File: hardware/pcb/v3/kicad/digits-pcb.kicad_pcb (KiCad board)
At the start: 2 copper layers, 61.9 x 76.2 mm, 77 parts, among them J8 Conn_01x04, SW1 Hook_DPDT, SW2 SW_Push, U10 XL6019E1, U2 DRV8871DDAR, U3 RP2040, U4 W25Q16JVSSIQ, U5 AMS1117-3.3, U6 TLV320AIC3104IRHBR, U7 XC6206P182MR, Y1 ABM8-272-T3

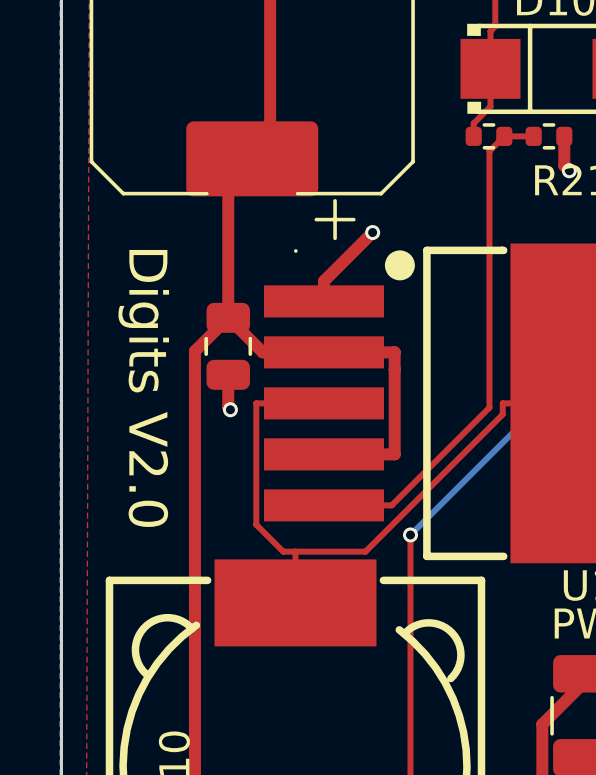
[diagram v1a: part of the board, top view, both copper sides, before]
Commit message: chore(hardware): update board silkscreen version label to V3
The F.SilkS title still read "Digits V2.0" after the promotion to V3.
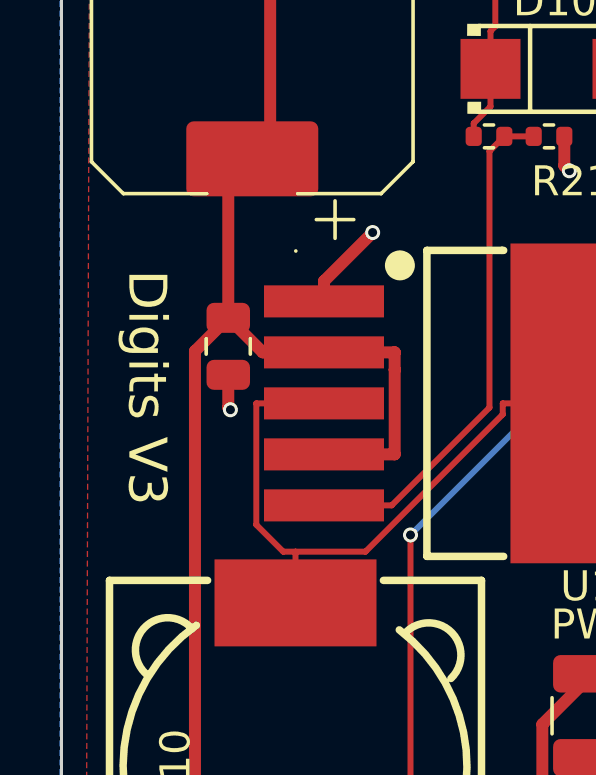
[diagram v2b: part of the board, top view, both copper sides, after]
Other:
- board text added: "Digits V3"
- board text removed: "Digits V2.0"
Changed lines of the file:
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@@
 		)
 	)
-	(gr_text "Digits V2.0"
+	(gr_text "Digits V3"
 		(at 15.598989 48.085455 270)
 		(layer "F.SilkS")

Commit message: fix(hardware): rate C55 for the 37V boost rail, assign SW2 BOOTSEL part
C55 was a 25V electrolytic on VBOOST (37.25V), which would over-volt and
fail. It is local VM decoupling, not the rail source (the XL6019 regulates
37V and C100's 100uF is the bulk reservoir), so dropping it to 10uF/50V
(C116402) in the same 5mm footprint keeps the decoupling ample with no
layout change. Also assign the SW2 6mm tactile (OMRON B3F-1002, C87036)
so the BOOTSEL button places.

DRC stays clean: 0 errors, 0 unconnected, 0 schematic-parity.
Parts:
- C55: value 47uF -> 10uF
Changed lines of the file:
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@@
 			)
 		)
-		(property "LCSC Part #" "C25102"
-			(at 0 0 0)
-			(unlocked yes)
+		(property "Value" "300"
+			(at 0 1.17 0)
 			(layer "F.Fab")
-			(hide yes)
 			(effects
 				(font
@@
 			)
 		)
-		(property "Value" "300"
-			(at 0 1.17 0)
+		(property "Datasheet" "~"
+			(at 0 0 0)
 			(layer "F.Fab")
+			(hide yes)
 			(effects
 				(font
-					(size 1 1)
-					(thickness 0.15)
+					(size 1.27 1.27)
 				)
 			)
 		)
-		(property "Datasheet" "~"
+		(property "Description" ""
 			(at 0 0 0)
 			(layer "F.Fab")
@@
 			)
 		)
-		(property "Description" ""
+		(property "LCSC Part #" "C25102"
 			(at 0 0 0)
+			(unlocked yes)
 			(layer "F.Fab")
 			(hide yes)
 			(effects
 				(font
-					(size 1.27 1.27)
+					(size 1 1)
+					(thickness 0.15)
 				)
 			)
@@
 			)
 		)
-		(property "LCSC Part #" "C2286"
-			(at 0 0 0)
-			(unlocked yes)
+		(property "Value" "LED_RED"
+			(at 0 1.43 0)
 			(layer "F.Fab")
-			(hide yes)
 			(effects
 				(font
@@
 			)
 		)
-		(property "Value" "LED_RED"
-			(at 0 1.43 0)
+		(property "Datasheet" "~"
+			(at 0 0 0)
 			(layer "F.Fab")
+			(hide yes)
 			(effects
 				(font
-					(size 1 1)
-					(thickness 0.15)
+					(size 1.27 1.27)
 				)
 			)
 		)
-		(property "Datasheet" "~"
+		(property "Description" ""
 			(at 0 0 0)
 			(layer "F.Fab")
@@
 			)
 		)
-		(property "Description" ""
+		(property "LCSC Part #" "C2286"
 			(at 0 0 0)
+			(unlocked yes)
 			(layer "F.Fab")
 			(hide yes)
 			(effects
 				(font
-					(size 1.27 1.27)
+					(size 1 1)
+					(thickness 0.15)
 				)
 			)
@@
 			)
 		)
-		(property "Value" "47uF"
+		(property "Value" "10uF"
 			(at 0 -3.7 90)
 			(layer "F.Fab")
@@
 			)
 		)
-		(property "LCSC Part #" "C336270"
+		(property "LCSC Part #" "C116402"
 			(at 0 0 270)
 			(unlocked yes)
@@
 			)
 		)
-		(property "LCSC Part #" "C12624"
-			(at 0 0 0)
-			(unlocked yes)
+		(property "Value" "LED_GREEN"
+			(at 0 1.43 0)
 			(layer "F.Fab")
-			(hide yes)
 			(effects
 				(font
@@
 			)
 		)
-		(property "Value" "LED_GREEN"
-			(at 0 1.43 0)
+		(property "Datasheet" "~"
+			(at 0 0 0)
 			(layer "F.Fab")
+			(hide yes)
 			(effects
 				(font
-					(size 1 1)
-					(thickness 0.15)
+					(size 1.27 1.27)
 				)
 			)
 		)
-		(property "Datasheet" "~"
+		(property "Description" ""
 			(at 0 0 0)
 			(layer "F.Fab")
@@
 			)
 		)
-		(property "Description" ""
+		(property "LCSC Part #" "C12624"
 			(at 0 0 0)
+			(unlocked yes)
 			(layer "F.Fab")
 			(hide yes)
 			(effects
 				(font
-					(size 1.27 1.27)
+					(size 1 1)
+					(thickness 0.15)
 				)
 			)
@@
 			)
 		)
-		(property "LCSC Part #" ""
+		(property "LCSC Part #" "C87036"
 			(at 0 0 270)
 			(unlocked yes)
@@
 			)
 		)
-		(property "LCSC Part #" "C25104"
-			(at 0 0 0)
-			(unlocked yes)
+		(property "Value" "330"
+			(at 0 1.17 0)
 			(layer "F.Fab")
-			(hide yes)
 			(effects
 				(font
@@
 			)
 		)
-		(property "Value" "330"
-			(at 0 1.17 0)
+		(property "Datasheet" "~"
+			(at 0 0 0)
 			(layer "F.Fab")
+			(hide yes)
 			(effects
 				(font
-					(size 1 1)
-					(thickness 0.15)
+					(size 1.27 1.27)
 				)
 			)
 		)
-		(property "Datasheet" "~"
+		(property "Description" ""
 			(at 0 0 0)
 			(layer "F.Fab")
@@
 			)
 		)
-		(property "Description" ""
+		(property "LCSC Part #" "C25104"
 			(at 0 0 0)
+			(unlocked yes)
 			(layer "F.Fab")
 			(hide yes)
 			(effects
 				(font
-					(size 1.27 1.27)
+					(size 1 1)
+					(thickness 0.15)
 				)
 			)

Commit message: fix(hardware): make the +3V3 green indicator reliable (D3, R13)
The emerald-green D3 (Vf ~3.1V) had only ~0.2V of headroom on the 3.3V
rail, so it would barely light and vary part-to-part. Switch to a low-Vf
yellow-green LED (KT-0603YG, C2289) and resize R13 to 120 ohm (C25752)
for ~10mA, matching the +5V red indicator. Same footprints, no re-route.
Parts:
- R13: value 330 -> 120
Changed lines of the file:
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@@
 			)
 		)
-		(property "LCSC Part #" "C12624"
+		(property "LCSC Part #" "C2289"
 			(at 0 0 0)
 			(unlocked yes)
@@
 			)
 		)
-		(property "Value" "330"
+		(property "Value" "120"
 			(at 0 1.17 0)
 			(layer "F.Fab")
@@
 			)
 		)
-		(property "LCSC Part #" "C25104"
+		(property "LCSC Part #" "C25752"
 			(at 0 0 0)
 			(unlocked yes)

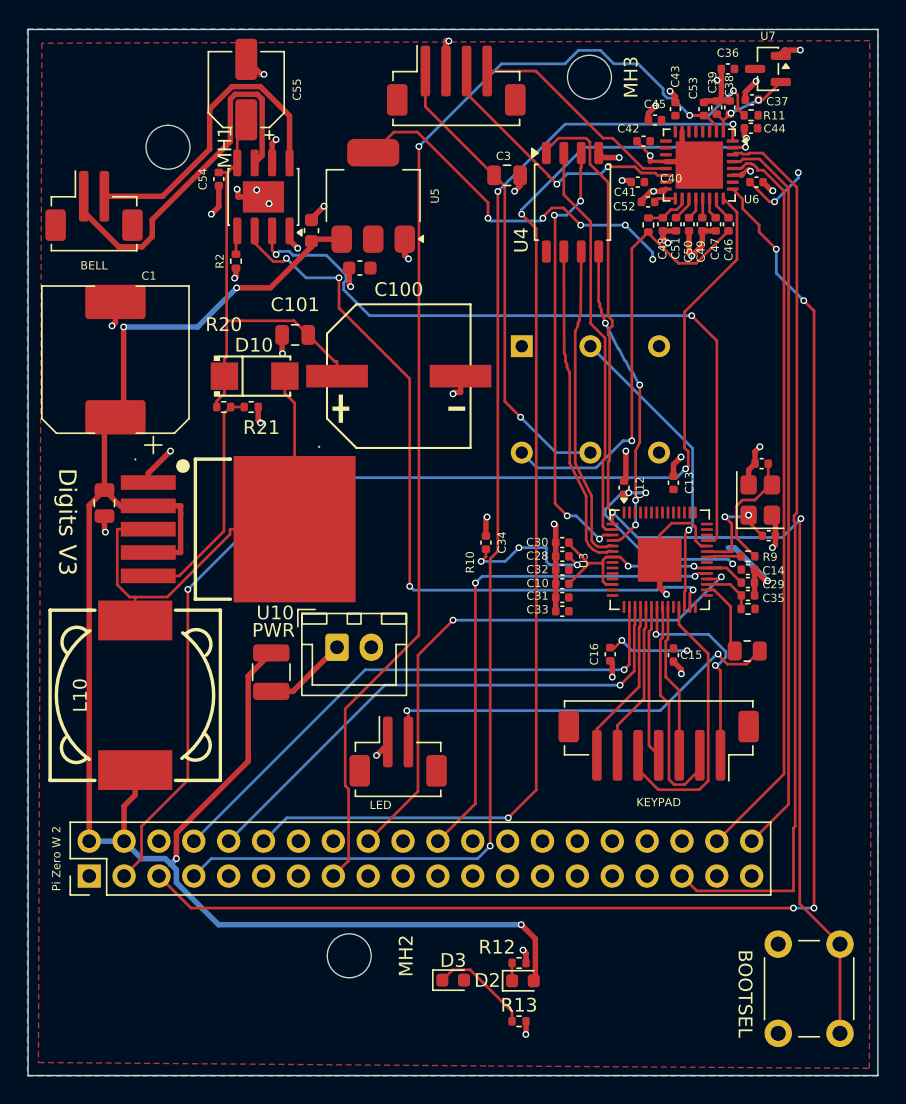
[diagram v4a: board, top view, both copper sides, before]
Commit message: fix(hardware): annotate connector refs (PWR1/LED1/etc.) for stable sync
KiCad's annotation during Update-PCB-from-Schematic numbered the un-annotated
semantic refs on the PCB: PWR->PWR1, LED->LED1, KEYPAD->KEYPAD1, BELL->BELL1,
Pi Zero W 2->Pi Zero W1. Sync the schematic and the production BOM to the same
forms so all three agree and schematic-parity is clean. The numbered refs are
valid annotations, so future re-syncs no longer re-mangle them.

DRC: 0 errors, 0 unconnected, 0 schematic-parity.
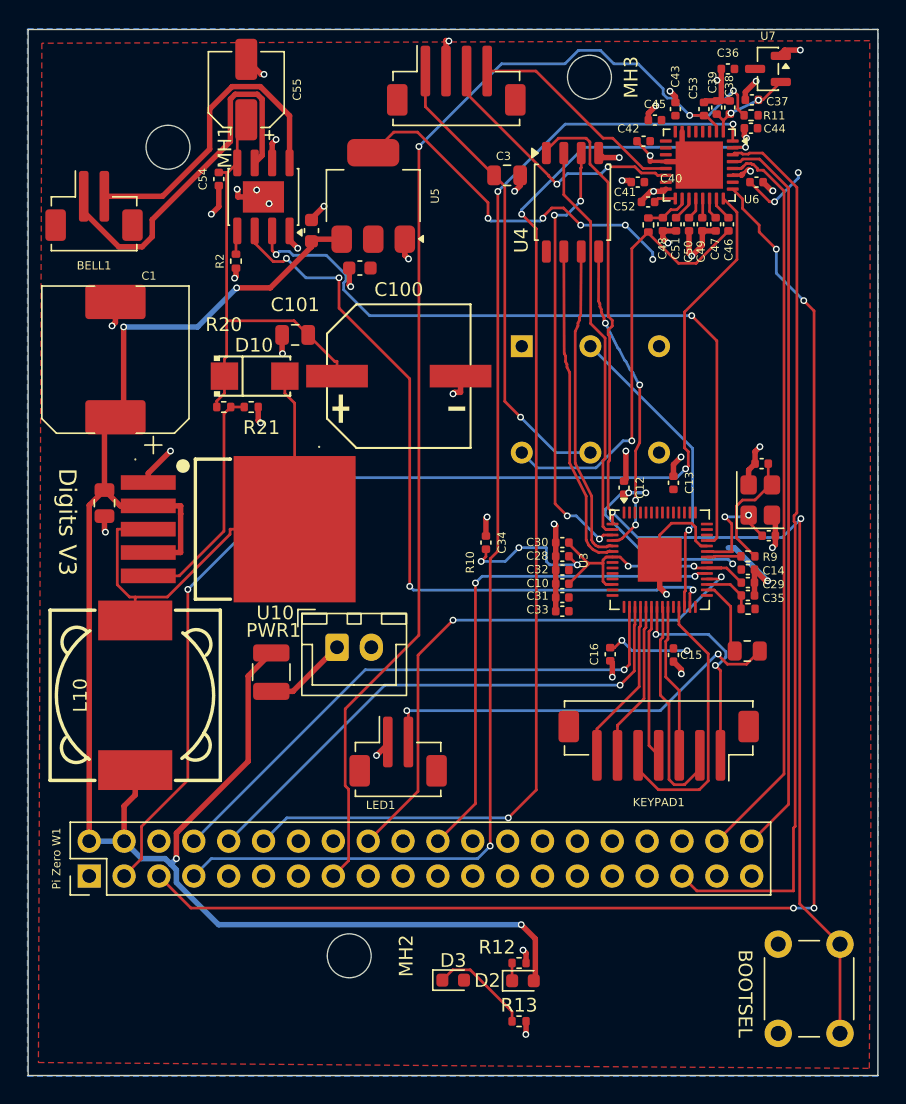
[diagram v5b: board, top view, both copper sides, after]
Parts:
- Pi Zero W1: renamed from Pi Zero W 2
- renumbered BELL to BELL1, KEYPAD to KEYPAD1, LED to LED1, PWR to PWR1
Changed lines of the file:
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@@
 		(descr "JST XH series connector, B2B-XH-A (http://www.jst-mfg.com/product/pdf/eng/eXH.pdf)")
 		(tags "connector JST XH vertical")
-		(property "Reference" "PWR"
+		(property "Reference" "PWR1"
 			(at -4.625 -1.225 0)
 			(layer "F.SilkS")
@@
 		(descr "Through hole straight pin header, 2x20, 2.54mm pitch, double rows")
 		(tags "Through hole pin header THT 2x20 2.54mm double row")
-		(property "Reference" "Pi Zero W 2"
+		(property "Reference" "Pi Zero W1"
 			(at 1.27 -2.38 90)
 			(layer "F.SilkS")
@@
 			(layers "*.Cu" "*.Mask")
 			(remove_unused_layers no)
-			(net "unconnected-(Pi Zero W 2-Pin_1-Pad1)")
+			(net "unconnected-(Pi Zero W1-Pin_1-Pad1)")
 			(pinfunction "Pin_1_1")
 			(pintype "passive+no_connect")
@@
 			(layers "*.Cu" "*.Mask")
 			(remove_unused_layers no)
-			(net "unconnected-(Pi Zero W 2-Pin_11-Pad11)")
+			(net "unconnected-(Pi Zero W1-Pin_11-Pad11)")
 			(pinfunction "Pin_11_11")
 			(pintype "passive+no_connect")
@@
 			(layers "*.Cu" "*.Mask")
 			(remove_unused_layers no)
-			(net "unconnected-(Pi Zero W 2-Pin_13-Pad13)")
+			(net "unconnected-(Pi Zero W1-Pin_13-Pad13)")
 			(pinfunction "Pin_13_13")
 			(pintype "passive+no_connect")
@@
 			(layers "*.Cu" "*.Mask")
 			(remove_unused_layers no)
-			(net "unconnected-(Pi Zero W 2-Pin_16-Pad16)")
+			(net "unconnected-(Pi Zero W1-Pin_16-Pad16)")
 			(pinfunction "Pin_16_16")
 			(pintype "passive+no_connect")
@@
 			(layers "*.Cu" "*.Mask")
 			(remove_unused_layers no)
-			(net "unconnected-(Pi Zero W 2-Pin_17-Pad17)")
+			(net "unconnected-(Pi Zero W1-Pin_17-Pad17)")
 			(pinfunction "Pin_17_17")
 			(pintype "passive+no_connect")
@@
 			(layers "*.Cu" "*.Mask")
 			(remove_unused_layers no)
-			(net "unconnected-(Pi Zero W 2-Pin_19-Pad19)")
+			(net "unconnected-(Pi Zero W1-Pin_19-Pad19)")
 			(pinfunction "Pin_19_19")
 			(pintype "passive+no_connect")
@@
 			(layers "*.Cu" "*.Mask")
 			(remove_unused_layers no)
-			(net "unconnected-(Pi Zero W 2-Pin_21-Pad21)")
+			(net "unconnected-(Pi Zero W1-Pin_21-Pad21)")
 			(pinfunction "Pin_21_21")
 			(pintype "passive+no_connect")
@@
 			(layers "*.Cu" "*.Mask")
 			(remove_unused_layers no)
-			(net "unconnected-(Pi Zero W 2-Pin_23-Pad23)")
+			(net "unconnected-(Pi Zero W1-Pin_23-Pad23)")
 			(pinfunction "Pin_23_23")
 			(pintype "passive+no_connect")
@@
 			(layers "*.Cu" "*.Mask")
 			(remove_unused_layers no)
-			(net "unconnected-(Pi Zero W 2-Pin_24-Pad24)")
+			(net "unconnected-(Pi Zero W1-Pin_24-Pad24)")
 			(pinfunction "Pin_24_24")
 			(pintype "passive+no_connect")
@@
 			(layers "*.Cu" "*.Mask")
 			(remove_unused_layers no)
-			(net "unconnected-(Pi Zero W 2-Pin_26-Pad26)")
+			(net "unconnected-(Pi Zero W1-Pin_26-Pad26)")
 			(pinfunction "Pin_26_26")
 			(pintype "passive+no_connect")
@@
 			(layers "*.Cu" "*.Mask")
 			(remove_unused_layers no)
-			(net "unconnected-(Pi Zero W 2-Pin_27-Pad27)")
+			(net "unconnected-(Pi Zero W1-Pin_27-Pad27)")
 			(pinfunction "Pin_27_27")
 			(pintype "passive+no_connect")
@@
 			(layers "*.Cu" "*.Mask")
 			(remove_unused_layers no)
-			(net "unconnected-(Pi Zero W 2-Pin_28-Pad28)")
+			(net "unconnected-(Pi Zero W1-Pin_28-Pad28)")
 			(pinfunction "Pin_28_28")
 			(pintype "passive+no_connect")
@@
 			(layers "*.Cu" "*.Mask")
 			(remove_unused_layers no)
-			(net "unconnected-(Pi Zero W 2-Pin_29-Pad29)")
+			(net "unconnected-(Pi Zero W1-Pin_29-Pad29)")
 			(pinfunction "Pin_29_29")
 			(pintype "passive+no_connect")
@@
 			(layers "*.Cu" "*.Mask")
 			(remove_unused_layers no)
-			(net "unconnected-(Pi Zero W 2-Pin_31-Pad31)")
+			(net "unconnected-(Pi Zero W1-Pin_31-Pad31)")
 			(pinfunction "Pin_31_31")
 			(pintype "passive+no_connect")
@@
 			(layers "*.Cu" "*.Mask")
 			(remove_unused_layers no)
-			(net "unconnected-(Pi Zero W 2-Pin_32-Pad32)")
+			(net "unconnected-(Pi Zero W1-Pin_32-Pad32)")
 			(pinfunction "Pin_32_32")
 			(pintype "passive+no_connect")
@@
 			(layers "*.Cu" "*.Mask")
 			(remove_unused_layers no)
-			(net "unconnected-(Pi Zero W 2-Pin_33-Pad33)")
+			(net "unconnected-(Pi Zero W1-Pin_33-Pad33)")
 			(pinfunction "Pin_33_33")
 			(pintype "passive+no_connect")
@@
 			(layers "*.Cu" "*.Mask")
 			(remove_unused_layers no)
-			(net "unconnected-(Pi Zero W 2-Pin_36-Pad36)")
+			(net "unconnected-(Pi Zero W1-Pin_36-Pad36)")
 			(pinfunction "Pin_36_36")
 			(pintype "passive+no_connect")
@@
 			(layers "*.Cu" "*.Mask")
 			(remove_unused_layers no)
-			(net "unconnected-(Pi Zero W 2-Pin_37-Pad37)")
+			(net "unconnected-(Pi Zero W1-Pin_37-Pad37)")
 			(pinfunction "Pin_37_37")
 			(pintype "passive+no_connect")
@@
 		(descr "JST ZH series connector, B2B-ZR-SM4-TF (http://www.jst-mfg.com/product/pdf/eng/eZH.pdf)")
 		(tags "connector JST ZH vertical")
-		(property "Reference" "BELL"
+		(property "Reference" "BELL1"
 			(at 0 4.35 0)
 			(layer "F.SilkS")
@@
 		(descr "JST ZH series connector, B7B-ZR-SM4-TF (http://www.jst-mfg.com/product/pdf/eng/eZH.pdf)")
 		(tags "connector JST ZH vertical")
-		(property "Reference" "KEYPAD"
+		(property "Reference" "KEYPAD1"
 			(at 0 -4.1245 0)
 			(layer "F.SilkS")
@@
 		(descr "JST ZH series connector, B2B-ZR-SM4-TF (http://www.jst-mfg.com/product/pdf/eng/eZH.pdf)")
 		(tags "connector JST ZH vertical")
-		(property "Reference" "LED"
+		(property "Reference" "LED1"
 			(at -1.275 3.9 0)
 			(layer "F.SilkS")
